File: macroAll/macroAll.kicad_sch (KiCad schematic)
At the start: 0 parts

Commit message: added remaining libraries and set up sheets
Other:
- added sheet Left (side.kicad_sch)
- added sheet Right (side.kicad_sch)
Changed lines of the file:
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@@
 	(generator_version "9.0")
 	(paper "A4")
+	(sheet
+		(at 59.69 60.96)
+		(size 95.25 60.96)
+		(exclude_from_sim no)
+		(in_bom yes)
+		(on_board yes)
+		(dnp no)
+		(fields_autoplaced yes)
+		(stroke
+			(width 0.1524)
+			(type solid)
+		)
+		(fill
+			(color 0 0 0 0.0000)
+		)
+		(property "Sheetname" "Left"
+			(at 59.69 60.2484 0)
+			(effects
+				(font
+					(size 1.27 1.27)
+				)
+				(justify left bottom)
+			)
+		)
+		(property "Sheetfile" "side.kicad_sch"
+			(at 59.69 122.5046 0)
+			(effects
+				(font
+					(size 1.27 1.27)
+				)
+				(justify left top)
+			)
+		)
+		(instances
+			(project "macroAll"
+				(path "/5c0825d9-c716-4482-b15b-296a0b2326a0"
+					(page "2")
+				)
+			)
+		)
+	)
+	(sheet
+		(at 170.18 60.96)
+		(size 90.17 60.96)
+		(exclude_from_sim no)
+		(in_bom yes)
+		(on_board yes)
+		(dnp no)
+		(fields_autoplaced yes)
+		(stroke
+			(width 0.1524)
+			(type solid)
+		)
+		(fill
+			(color 0 0 0 0.0000)
+		)
+		(property "Sheetname" "Right"
+			(at 170.18 60.2484 0)
+			(effects
+				(font
+					(size 1.27 1.27)
+				)
+				(justify left bottom)
+			)
+		)
+		(property "Sheetfile" "side.kicad_sch"
+			(at 170.18 122.5046 0)
+			(effects
+				(font
+					(size 1.27 1.27)
+				)
+				(justify left top)
+			)
+		)
+		(instances
+			(project "macroAll"
+				(path "/5c0825d9-c716-4482-b15b-296a0b2326a0"
+					(page "3")
+				)
+			)
+		)
+	)
 	(sheet_instances
 		(path "/"

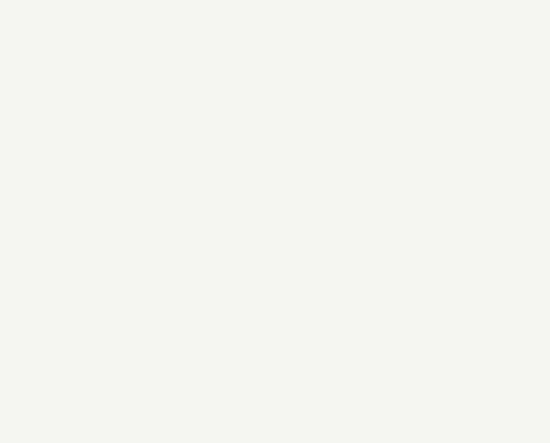
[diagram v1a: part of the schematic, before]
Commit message: added circuitry
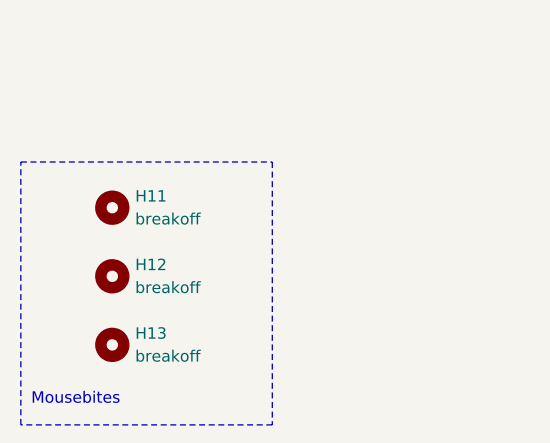
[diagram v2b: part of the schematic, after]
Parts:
- added H11, H12, H13: breakoff, symbol Mechanical:MountingHole
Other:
- note added: "Mousebites"
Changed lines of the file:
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@@
 	(generator_version "9.0")
 	(paper "A4")
+	(rectangle
+		(start 59.69 154.94)
+		(end 87.63 184.15)
+		(stroke
+			(width 0)
+			(type dash)
+		)
+		(fill
+			(type none)
+		)
+	)
+	(text "Mousebites\n\n"
+		(exclude_from_sim no)
+		(at 65.786 182.372 0)
+		(effects
+			(font
+				(size 1.27 1.27)
+			)
+		)
+	)
+	(symbol
+		(lib_id "Mechanical:MountingHole")
+		(at 69.85 167.64 0)
+		(unit 1)
+		(exclude_from_sim no)
+		(in_bom no)
+		(on_board yes)
+		(dnp no)
+		(fields_autoplaced yes)
+		(property "Reference" "H12"
+			(at 72.39 166.3699 0)
+			(effects
+				(font
+					(size 1.27 1.27)
+				)
+				(justify left)
+			)
+		)
+		(property "Value" "breakoff"
+			(at 72.39 168.9099 0)
+			(effects
+				(font
+					(size 1.27 1.27)
+				)
+				(justify left)
+			)
+		)
+		(property "Footprint" ""
+			(at 69.85 167.64 0)
+			(effects
+				(font
+					(size 1.27 1.27)
+				)
+				(hide yes)
+			)
+		)
+		(property "Datasheet" "~"
+			(at 69.85 167.64 0)
+			(effects
+				(font
+					(size 1.27 1.27)
+				)
+				(hide yes)
+			)
+		)
+		(property "Description" "Mounting Hole without connection"
+			(at 69.85 167.64 0)
+			(effects
+				(font
+					(size 1.27 1.27)
+				)
+				(hide yes)
+			)
+		)
+		(instances
+			(project ""
+				(path "/5c0825d9-c716-4482-b15b-296a0b2326a0"
+					(reference "H12")
+					(unit 1)
+				)
+			)
+		)
+	)
+	(symbol
+		(lib_id "Mechanical:MountingHole")
+		(at 69.85 175.26 0)
+		(unit 1)
+		(exclude_from_sim no)
+		(in_bom no)
+		(on_board yes)
+		(dnp no)
+		(fields_autoplaced yes)
+		(property "Reference" "H13"
+			(at 72.39 173.9899 0)
+			(effects
+				(font
+					(size 1.27 1.27)
+				)
+				(justify left)
+			)
+		)
+		(property "Value" "breakoff"
+			(at 72.39 176.5299 0)
+			(effects
+				(font
+					(size 1.27 1.27)
+				)
+				(justify left)
+			)
+		)
+		(property "Footprint" ""
+			(at 69.85 175.26 0)
+			(effects
+				(font
+					(size 1.27 1.27)
+				)
+				(hide yes)
+			)
+		)
+		(property "Datasheet" "~"
+			(at 69.85 175.26 0)
+			(effects
+				(font
+					(size 1.27 1.27)
+				)
+				(hide yes)
+			)
+		)
+		(property "Description" "Mounting Hole without connection"
+			(at 69.85 175.26 0)
+			(effects
+				(font
+					(size 1.27 1.27)
+				)
+				(hide yes)
+			)
+		)
+		(instances
+			(project ""
+				(path "/5c0825d9-c716-4482-b15b-296a0b2326a0"
+					(reference "H13")
+					(unit 1)
+				)
+			)
+		)
+	)
+	(symbol
+		(lib_id "Mechanical:MountingHole")
+		(at 69.85 160.02 0)
+		(unit 1)
+		(exclude_from_sim no)
+		(in_bom no)
+		(on_board yes)
+		(dnp no)
+		(fields_autoplaced yes)
+		(property "Reference" "H11"
+			(at 72.39 158.7499 0)
+			(effects
+				(font
+					(size 1.27 1.27)
+				)
+				(justify left)
+			)
+		)
+		(property "Value" "breakoff"
+			(at 72.39 161.2899 0)
+			(effects
+				(font
+					(size 1.27 1.27)
+				)
+				(justify left)
+			)
+		)
+		(property "Footprint" ""
+			(at 69.85 160.02 0)
+			(effects
+				(font
+					(size 1.27 1.27)
+				)
+				(hide yes)
+			)
+		)
+		(property "Datasheet" "~"
+			(at 69.85 160.02 0)
+			(effects
+				(font
+					(size 1.27 1.27)
+				)
+				(hide yes)
+			)
+		)
+		(property "Description" "Mounting Hole without connection"
+			(at 69.85 160.02 0)
+			(effects
+				(font
+					(size 1.27 1.27)
+				)
+				(hide yes)
+			)
+		)
+		(instances
+			(project ""
+				(path "/5c0825d9-c716-4482-b15b-296a0b2326a0"
+					(reference "H11")
+					(unit 1)
+				)
+			)
+		)
+	)
 	(sheet
 		(at 59.69 60.96)

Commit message: Changed circuit board used
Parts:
- H11, H12, H13: footprint (none) -> PanelizationPretty:mouse-bite-5mm-slot
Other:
- title: (none) -> marcoAll
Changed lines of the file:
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@@
 	(generator_version "9.0")
 	(paper "A4")
+	(title_block
+		(title "marcoAll")
+		(date "2025-11-03")
+	)
 	(rectangle
 		(start 59.69 154.94)
@@
 			)
 		)
-		(property "Footprint" ""
+		(property "Footprint" "PanelizationPretty:mouse-bite-5mm-slot"
 			(at 69.85 167.64 0)
 			(effects
@@
 			)
 		)
-		(property "Footprint" ""
+		(property "Footprint" "PanelizationPretty:mouse-bite-5mm-slot"
 			(at 69.85 175.26 0)
 			(effects
@@
 			)
 		)
-		(property "Footprint" ""
+		(property "Footprint" "PanelizationPretty:mouse-bite-5mm-slot"
 			(at 69.85 160.02 0)
 			(effects
